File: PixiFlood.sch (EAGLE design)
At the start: 37 parts, among them IC1 WS2811-SOP8, IC2 78L05Z, T1 2N3904, T2 2N3904, T3 2N3904, U1 PT4115B89E-A2, U2 PT4115B89E-A2, U3 PT4115B89E-A2, X1 22-23-2031, X2 22-23-2031

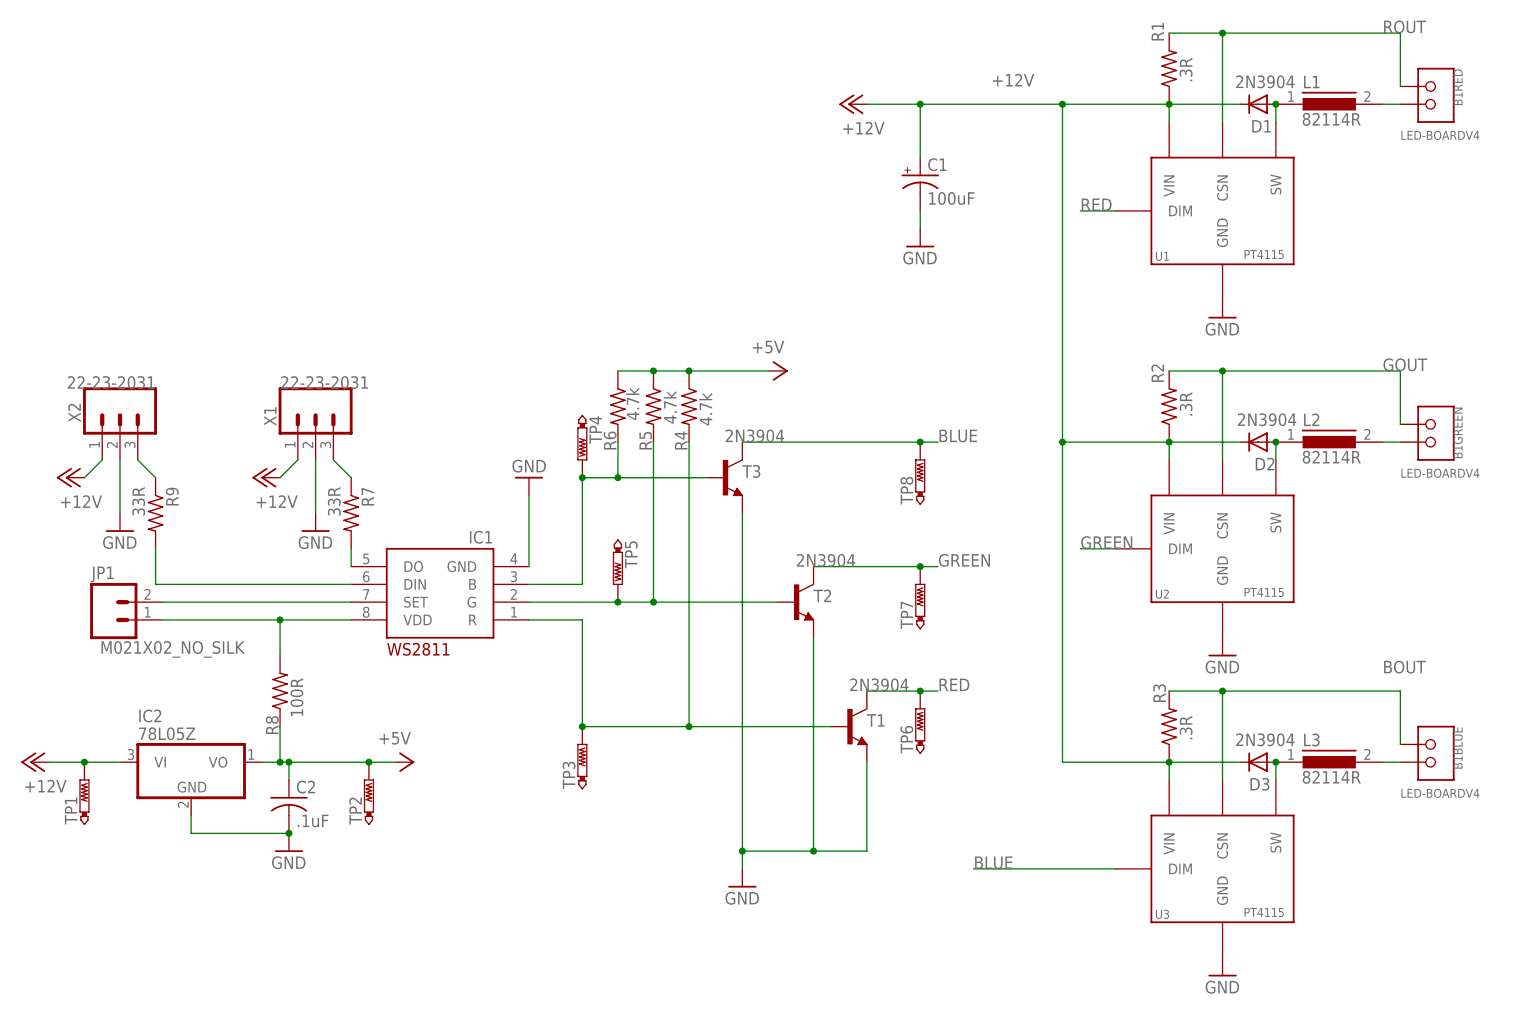
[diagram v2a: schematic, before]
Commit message: Reworked layout
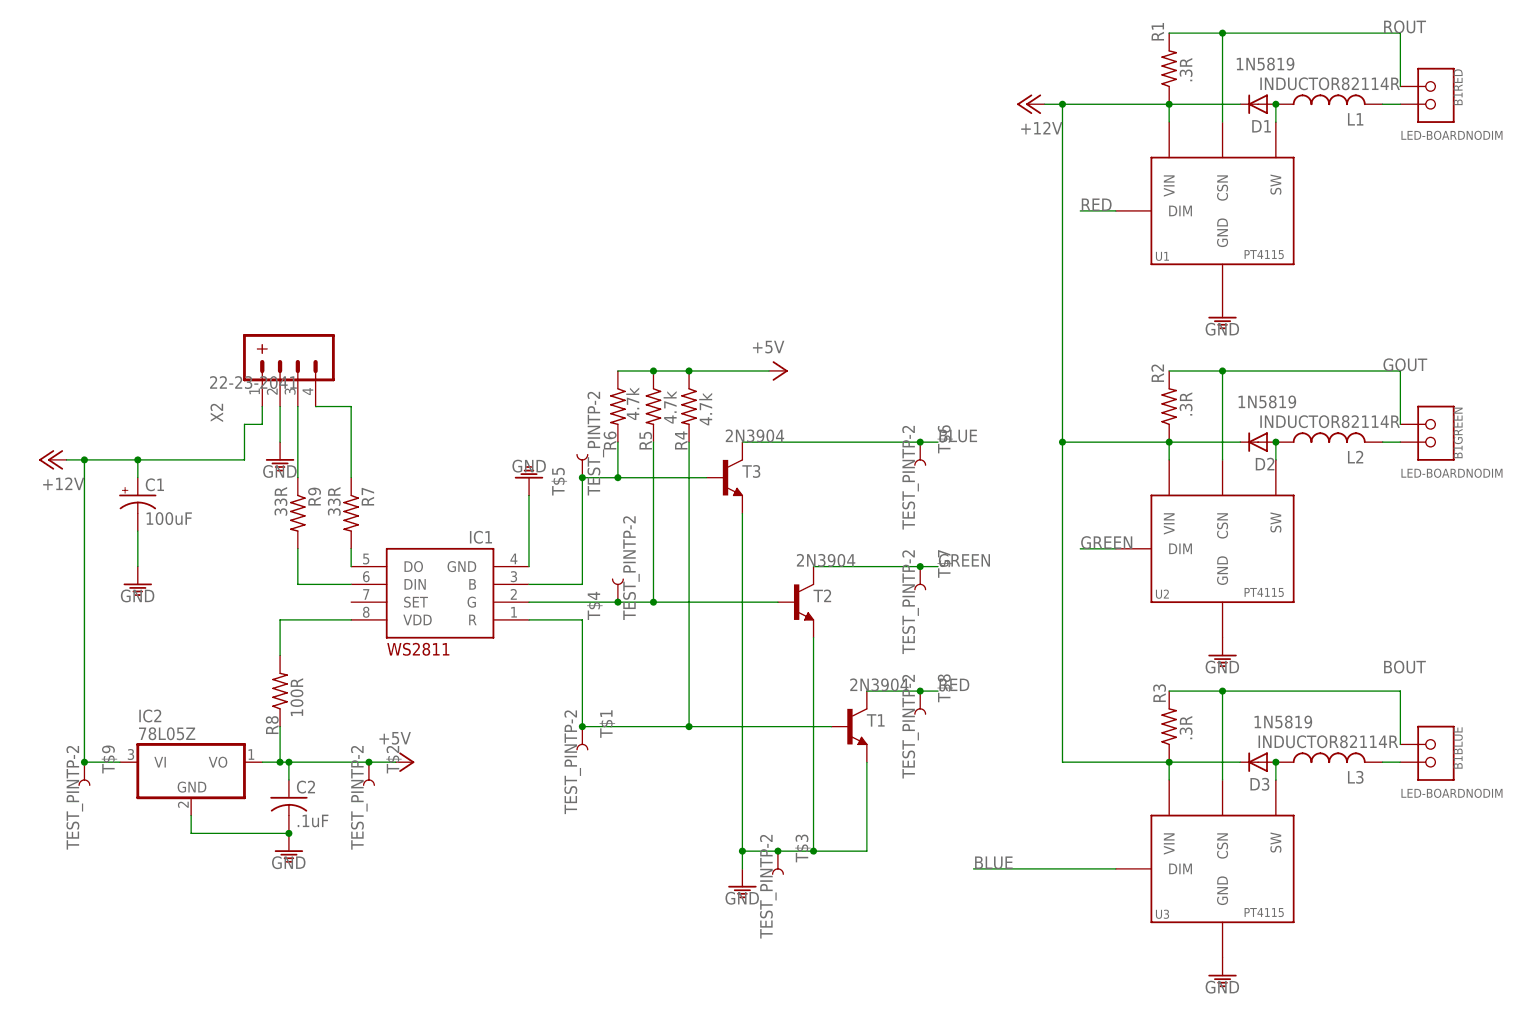
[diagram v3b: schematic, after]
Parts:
- removed JP1: M021X02_NO_SILK, SparkFun-Connectors:M021X02_NO_SILK
- removed TP1, TP2: PTR1B2,54, testpad:PTR1B2,54
- removed TP3, TP4, TP5, TP6, TP7, TP8: PTR1B1,27, testpad:PTR1B1,27
- removed X1: 22-23-2031, connectors:22-23-2031
- added T$1, T$2, T$3, T$4, T$5, T$6, T$7, T$8, T$9: TEST_PINTP-2, headers:TEST_PINTP-2
- B1: value LED-BOARDV4 -> LED-BOARDNODIM; device special:LED-BOARDV4 -> myBoards:LED-BOARDNODIM
- D1, D2, D3: value 2N3904 -> 1N5819
- L1, L2, L3: value 82114R -> INDUCTOR82114R; device inductors:82114R -> rcl:INDUCTOR82114R
- U1, U2, U3: value PT4115B89E-A2 -> PT4115B89E; device drivers:PT4115B89E-A2 -> drivers:PT4115B89E
- X2: value 22-23-2031 -> 22-23-2041; device connectors:22-23-2031 -> connectors:22-23-2041
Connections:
- net N$6 renamed DIN
- net N$7 renamed DO-R
- net N$8 renamed DIN-R
- removed net N$16: IC1.SET, JP1.2
- removed net N$4: R7.1, X1.3
- new net DO: R7.1, X2.4
- net +12V: now also T$9.1; no longer TP1.TP, X1.1
- net +5V: now also T$2.1; no longer TP2.TP
- net BLUE: now also T$6.1; no longer TP8.TP
- net GND: now also T$3.1; no longer X1.2
- net GREEN: now also T$7.1; no longer TP7.TP
- net N$15: now also T$5.1; no longer TP4.TP
- net N$18: now also T$4.1; no longer TP5.TP
- net N$20: now also T$1.1; no longer TP3.TP
- net RED: now also T$8.1; no longer TP6.TP
- net VDD: no longer JP1.1
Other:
- moved on the sheet: C1, R9

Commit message: Initial Commit
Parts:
- removed T$1, T$2, T$3, T$4, T$5, T$6, T$7, T$8, T$9: TEST_PINTP-2, headers:TEST_PINTP-2
- removed T1, T2, T3: 2N3904, transistor:2N3904
- removed X2: 22-23-2041, connectors:22-23-2041
- added C3: .1uF, capacitors:CAP_POL1206
- added C4: 10uF, capacitors:CAP_POLCASE-D
- added IC3: TC7W04FP-0.65, logic:TC7W04FP-0.65
- added TP1, TP2, TP3, TP4, TP5, TP6, TP7, TP9: TPSQTP15R, testpad:TPSQTP15R
- added TP8: TPSQTP20SQ, testpad:TPSQTP20SQ
- added X1: 22-23-2041, connectors:22-23-2041
- B1: value LED-BOARDNODIM -> LED-BOARDV4; device myBoards:LED-BOARDNODIM -> special:LED-BOARDV4
- C1: value 100uF -> 10uF; device rcl:CPOL-USTT2D6L -> capacitors:CAP_POLCASE-D
- C2: value .1uF -> 10uF; device rcl:C-US050-024X044 -> capacitors:CAP_POLCASE-D
- D1, D2, D3: value 1N5819 -> B340A; device diode:DIODE-DO07 -> SparkFun-DiscreteSemi:DIODE-SCHOTTKY-B340A
- IC1: value WS2811-SOP8 -> 78L05SMD; device MyLibrary:WS2811-SOP8 -> regulators:78L05SMD
- IC2: value 78L05Z -> WS2811S; device linear:78L05Z -> drivers:WS2811S
- L1, L2, L3: value INDUCTOR82114R -> SLF7045T-101MR60-H; device rcl:INDUCTOR82114R -> inductors:SLF7045
- R1: value .3R -> .33R; device resistor:R-US_0204/7 -> resistor:R-US_R1210
- R2, R3: value .3R -> 33R; device resistor:R-US_0204/7 -> rcl:R-US_R1206
- R4: value 4.7k -> 100; device resistor:R-US_0204/7 -> rcl:R-US_R1206
- R5, R6: value 4.7k -> .33R; device resistor:R-US_0204/7 -> resistor:R-US_R1210
- R7, R9: value 33R -> 4.7k; device rcl:R-US_0204/7 -> rcl:R-US_R1206
- R8: value 100R -> 4.7k; device rcl:R-US_0204/7 -> rcl:R-US_R1206
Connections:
- removed net +12V: C1.+, D1.C, D2.C, D3.C, IC2.VI, R1.1, R2.1, R3.1, T$9.1, U1.VIN, U2.VIN, U3.VIN, X2.1
- removed net DIN-R: IC1.DIN, R9.2
- removed net DO-R: IC1.DO, R7.2
- removed net N$15: IC1.B, R6.2, T$5.1, T3.B
- removed net N$18: IC1.G, R5.2, T$4.1, T2.B
- removed net N$20: IC1.R, R4.2, T$1.1, T1.B
- new net BLU-WS: IC2.B, IC3G$1.I, R7.2, TP2.TP
- new net DIN-E: R2.1, X1.3
- new net DO-E: R3.1, X1.4
- new net GREN-WS: IC2.G, IC3G$3.I, R8.2, TP3.TP
- new net RED-WS: IC2.R, IC3G$2.I, R9.2, TP7.TP
- new net VIN: C1.+, C2.+, C4.+, D1.C, D2.C, D3.C, IC1G$1.VIN, R1.2, R5.2, R6.2, TP4.TP, U1.VIN, U2.VIN, U3.VIN, X1.1
- net +5V: now also C3.+, IC1G$1.VOUT, IC3VCC.S, R7.1, R9.1, TP5.TP; no longer C2.1, IC2.VO, R5.1, R6.1, T$2.1
- net BLUE: now also IC3G$1.O, TP9.TP; no longer T$6.1, T3.C
- net BOUT: now also R6.1; no longer R3.2
- net DIN: now also IC2.DIN, R2.2; no longer R9.1, X2.3
- net DO: now also IC2.DO, R3.2; no longer R7.1, X2.4
- net GND: now also C2.-, C3.-, C4.-, IC1G$1.GND@2, IC3GND.S, TP8.TP, X1.2; no longer C2.2, IC1.GND, T$3.1, T1.E, T2.E, T3.E, X2.2
- net GOUT: now also R5.1; no longer R2.2
- net GREEN: now also IC3G$3.O, TP6.TP; no longer T$7.1, T2.C
- net RED: now also IC3G$2.O, TP1.TP; no longer T$8.1, T1.C
- net ROUT: now also R1.1; no longer R1.2
- net VDD: now also IC2.VDD, R4.2; no longer IC1.VDD, R8.2
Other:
- moved on the sheet: B1BLUE, B1GREEN, B1RED, C1, R1, R2, R3, R4, R5, R6, R7, R8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

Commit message: Reworked layout
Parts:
- added C10, C8, C9: 10uF, rcl:CPOL-USSMCD
- added C5, C7: 10uF, rcl:C-USC1206
- added C6: .1uF, rcl:C-USC0805
- added FB1: BLM21PG221SN1D, ELL-i-Passives:FB-0805-A
- added IC4: WS2811SOP8, drivers:WS2811SOP8
- added IC5: TC7W04FP-0.65, logic:TC7W04FP-0.65
- added J1: (no value), connectors:M04X2A
- added JP1, JP2: (no value), connectors:M03LOCK
- added JP3: M02NO_SILK, connectors:M02NO_SILK
- added JP5: (no value), connectors:M03LOCK_NO_SILK
- added R10, R11: 4.7kohm, rcl:R-US_M0805
- added S1, S2: SP, switch:TACT
- added TP10, TP11, TP12, TP13, TP14, TP15, TP16: TPSQPAD1-13, testpad:TPSQPAD1-13
- B1: value LED-BOARDV4 -> LED-BOARDRF; device special:LED-BOARDV4 -> myBoards:LED-BOARDRF
- C1: value 10uF -> (none); device capacitors:CAP_POLCASE-D -> rcl:CPOL-USUD-6,3X5,8
- C2: device capacitors:CAP_POLCASE-D -> rcl:C-USC1206
- C3: value .1uF -> 10uF; device capacitors:CAP_POL1206 -> rcl:C-USC1206
- C4: value 10uF -> .1uF; device capacitors:CAP_POLCASE-D -> rcl:C-USC0805
- D1, D2, D3: value B340A -> MBRA140; device SparkFun-DiscreteSemi:DIODE-SCHOTTKY-B340A -> SparkFun-DiscreteSemi:DIODE-SCHOTTKY-MBRA140
- IC1: value 78L05SMD -> L78LXXCU/BU; device regulators:78L05SMD -> regulators:L78LXXCU/BU
- IC2: value WS2811S -> 74LVC1G125DBV; device drivers:WS2811S -> logic:74LVC1G125DBV
- IC3: value TC7W04FP-0.65 -> LM1117-SOT223; device logic:TC7W04FP-0.65 -> regulators:LM1117-SOT223
- R1: value .33R -> 10K; device resistor:R-US_R1210 -> resistors:R-US_R0805
- R2: value 33R -> 10K; device rcl:R-US_R1206 -> resistors:R-US_R0805
- R3: value 33R -> 100ohm; device rcl:R-US_R1206 -> rcl:R-US_M0805
- R4: value 100 -> 33R; device rcl:R-US_R1206 -> rcl:R-US_M1206
- R5: value .33R -> 100; device resistor:R-US_R1210 -> resistors:R-US_R0805
- R6: value .33R -> .3ohm .25w; device resistor:R-US_R1210 -> rcl:R-US_R1210
- R7: value 4.7k -> .3hm .25w; device rcl:R-US_R1206 -> rcl:R-US_R1210
- R8: value 4.7k -> .3ohm .25w; device rcl:R-US_R1206 -> rcl:R-US_R1210
- R9: value 4.7k -> 4.7kohm; device rcl:R-US_R1206 -> rcl:R-US_M0805
- TP1, TP2, TP3, TP4, TP5, TP6, TP7, TP9: value TPSQTP15R -> TPSQPAD1-13; device testpad:TPSQTP15R -> testpad:TPSQPAD1-13
- TP8: value TPSQTP20SQ -> TPSQPAD1-13; device testpad:TPSQTP20SQ -> testpad:TPSQPAD1-13
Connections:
- removed net BLU-WS: IC2.B, IC3G$1.I, R7.2, TP2.TP
- removed net DIN-E: R2.1, X1.3
- removed net DO-E: R3.1, X1.4
- removed net GREN-WS: IC2.G, IC3G$3.I, R8.2, TP3.TP
- removed net N$10: B1BLUE.P$1, L3.2
- removed net N$9: B1GREEN.P$1, L2.2
- removed net RED-WS: IC2.R, IC3G$2.I, R9.2, TP7.TP
- removed net VIN: C1.+, C2.+, C4.+, D1.C, D2.C, D3.C, IC1G$1.VIN, R1.2, R5.2, R6.2, TP4.TP, U1.VIN, U2.VIN, U3.VIN, X1.1
- new net +12V: C1.+, C10.+, C8.+, C9.+, D1.C, D2.C, D3.C, IC1.IN, R6.2, R7.2, R8.2, TP10.TP, U1.VIN, U2.VIN, U3.VIN, X1.4
- new net +3V3: C5.1, FB1.1, IC3.HEATSINK, IC3.VOUT, R1.2, R2.1, TP4.TP
- new net DIN-W: R4.1, X1.1
- new net GPIO0: J1.6, R1.1, S2.P
- new net GPIO2: IC2A.I, J1.4
- new net LED-B-NEG: B1BLUE.P$1, L3.2, TP6.TP
- new net LED-G-NEG: B1GREEN.P$1, L2.2, TP8.TP
- new net LED-R-NEG: B1RED.P$1, L1.2, TP9.TP
- new net N$16: IC4.B, IC5G$1.I, R9.2, TP14.TP
- new net N$4: IC4.G, IC5G$3.I, R11.2, TP15.TP
- new net N$6: IC2A.O, R5.2
- new net RST: J1.5, R2.2, S1.P
- new net RX: J1.8, JP1.2
- new net TX: J1.1, JP1.3
- new net VCC: C7.1, FB1.2, J1.3, J1.7
- new net WIFI: JP2.3, R5.1
- new net WIRED: JP2.1, R4.2
- net +5V: now also C2.1, C3.1, C4.1, C6.1, IC1.OUT, IC2VCC.S, IC3.VIN, IC5VCC.S, R10.1, R11.1, R3.2, TP1.TP; no longer C3.+, IC1G$1.VOUT, IC3VCC.S, R4.1, R7.1, R8.1, TP5.TP
- net BLUE: now also IC5G$1.O, TP11.TP; no longer IC3G$1.O, TP9.TP
- net BOUT: now also R8.1, TP7.TP; no longer R6.1
- net DIN: now also IC4.DIN, JP2.2; no longer IC2.DIN, R2.2
- net DO: now also IC4.DO, X1.2; no longer IC2.DO, R3.2
- net GND: now also C10.-, C2.2, C3.2, C4.2, C5.2, C6.2, C7.2, C8.-, C9.-, IC1.GND, IC1.GND1, IC2A.OE, IC2GND.S, IC3.GND, IC4.GND, IC5GND.S, J1.2, JP1.1, JP3.1, JP3.2, JP5.1, JP5.2, JP5.3, S1.S, S2.S, TP2.TP, X1.3; no longer C2.-, C3.-, C4.-, IC1G$1.GND@2, IC2.GND, IC3GND.S, TP8.TP, X1.2
- net GOUT: now also R7.1, TP5.TP; no longer R5.1
- net GREEN: now also IC5G$3.O, TP12.TP; no longer IC3G$3.O, TP6.TP
- net N$3: now also IC4.R, IC5G$2.I, R10.2, TP16.TP; no longer B1RED.P$1, L1.2
- net RED: now also IC5G$2.O, TP13.TP; no longer IC3G$2.O, TP1.TP
- net ROUT: now also R6.1, TP3.TP; no longer R1.1
- net VDD: now also IC4.VDD, R3.1; no longer IC2.VDD, R4.2
